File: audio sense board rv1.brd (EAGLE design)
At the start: 130.8 x 26.7 mm, 33 parts, among them IC2 TSOP38238, J1 PJRAN1X1U01X, J2 PJRAN1X1U01X, Q1 2N3904, Q2 2N3904

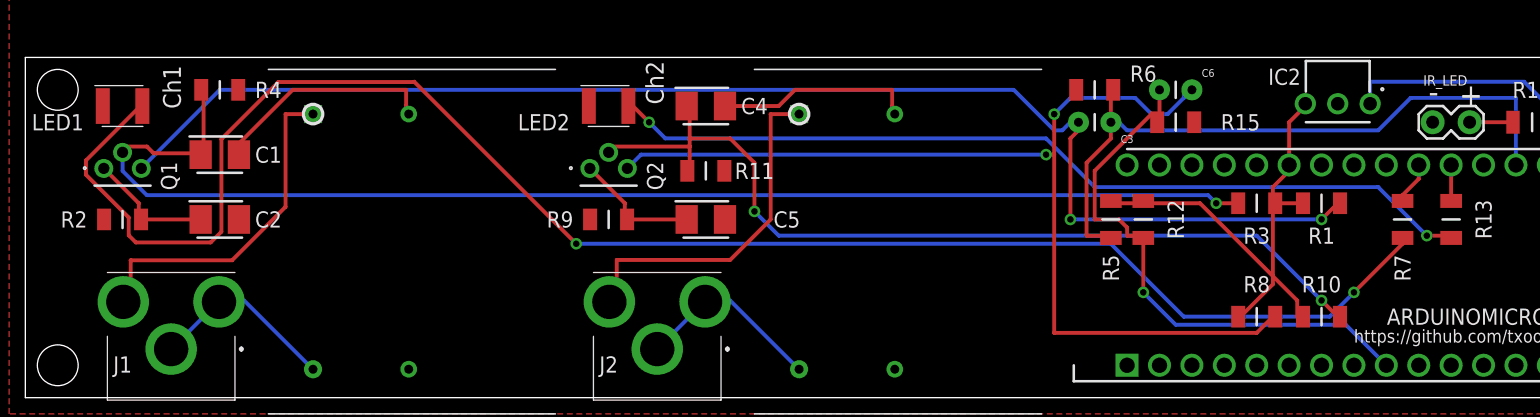
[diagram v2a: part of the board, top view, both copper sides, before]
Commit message: increase pad size for all resistors
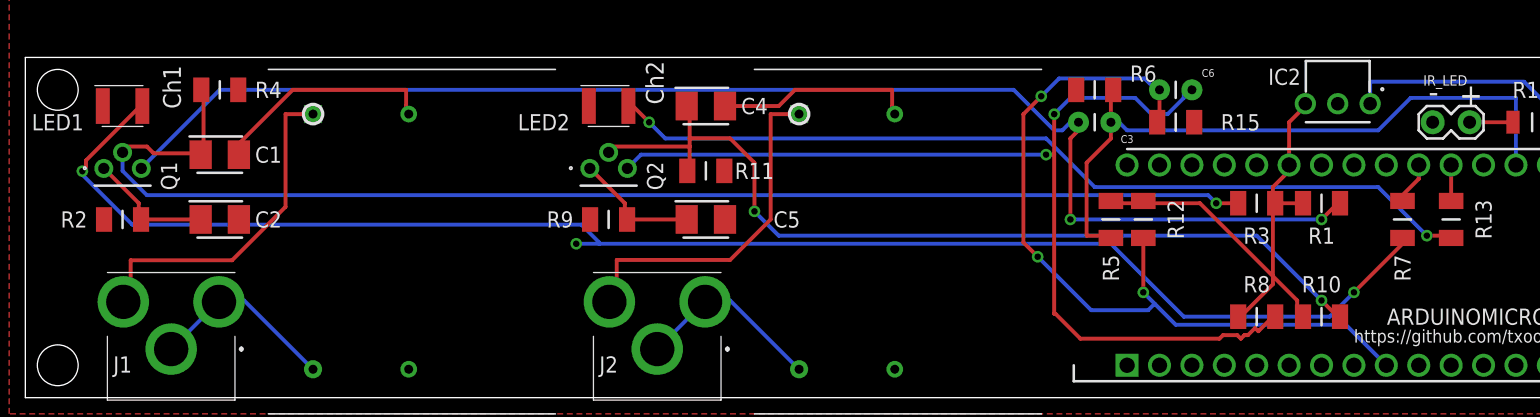
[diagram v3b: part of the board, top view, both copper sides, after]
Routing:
- net CHAN2: track 44.7 -> 64.0 mm, vias 1 -> 3
- net N$4: track 133.4 -> 120.3 mm, vias 2 -> 3
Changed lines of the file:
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@@
 <layers>
 <layer number="1" name="Top" color="4" fill="1" visible="yes" active="yes"/>
-<layer number="16" name="Bottom" color="1" fill="1" visible="no" active="yes"/>
+<layer number="16" name="Bottom" color="1" fill="1" visible="yes" active="yes"/>
 <layer number="17" name="Pads" color="2" fill="1" visible="yes" active="yes"/>
 <layer number="18" name="Vias" color="2" fill="1" visible="yes" active="yes"/>
@@
 <contactref element="R15" pad="2"/>
 <contactref element="C6" pad="1"/>
-<wire x1="86.36" y1="11.43" x2="87.63" y2="11.43" width="0.3048" layer="1"/>
-<wire x1="86.36" y1="12.065" x2="86.36" y2="11.43" width="0.3048" layer="1"/>
-<wire x1="85.725" y1="12.7" x2="86.36" y2="12.065" width="0.3048" layer="1"/>
-<wire x1="83.82" y1="12.7" x2="85.725" y2="12.7" width="0.3048" layer="1"/>
-<wire x1="83.82" y1="16.51" x2="83.82" y2="12.7" width="0.3048" layer="1"/>
-<wire x1="88.265" y1="20.955" x2="83.82" y2="16.51" width="0.3048" layer="1"/>
-<wire x1="88.9" y1="20.955" x2="88.265" y2="20.955" width="0.3048" layer="1"/>
 <wire x1="88.9" y1="20.32" x2="88.9" y2="20.955" width="0.3048" layer="1"/>
-<wire x1="87.63" y1="11.43" x2="87.63" y2="11.25" width="0.3048" layer="1"/>
 <wire x1="88.9" y1="20.32" x2="88.72" y2="20.32" width="0.3048" layer="1"/>
 <wire x1="88.9" y1="20.955" x2="88.9" y2="22.86" width="0.3048" layer="1"/>
@@
 <wire x1="103.505" y1="4.445" x2="106.68" y2="1.27" width="0.3048" layer="16"/>
 <wire x1="90.17" y1="4.445" x2="103.505" y2="4.445" width="0.3048" layer="16"/>
-<wire x1="87.63" y1="6.985" x2="90.17" y2="4.445" width="0.3048" layer="16"/>
+<wire x1="87.63" y1="6.985" x2="88.519" y2="6.096" width="0.3048" layer="16"/>
+<wire x1="88.519" y1="6.096" x2="90.17" y2="4.445" width="0.3048" layer="16"/>
 <wire x1="87.63" y1="11.25" x2="87.63" y2="6.985" width="0.3048" layer="1"/>
 <via x="87.63" y="6.985" extent="1-16" drill="0.508"/>
+<wire x1="88.5698" y1="22.9108" x2="88.8492" y2="22.9108" width="0.3048" layer="16"/>
+<wire x1="87.7316" y1="23.749" x2="88.5698" y2="22.9108" width="0.3048" layer="16"/>
+<wire x1="81.026" y1="23.749" x2="87.7316" y2="23.749" width="0.3048" layer="16"/>
+<wire x1="79.629" y1="22.352" x2="81.026" y2="23.749" width="0.3048" layer="16"/>
+<wire x1="78.232" y1="20.955" x2="79.629" y2="22.352" width="0.3048" layer="1"/>
+<wire x1="78.232" y1="10.8966" x2="78.232" y2="20.955" width="0.3048" layer="1"/>
+<wire x1="79.3496" y1="9.779" x2="78.232" y2="10.8966" width="0.3048" layer="1"/>
+<wire x1="83.5406" y1="5.588" x2="79.3496" y2="9.779" width="0.3048" layer="16"/>
+<wire x1="88.011" y1="5.588" x2="83.5406" y2="5.588" width="0.3048" layer="16"/>
+<wire x1="88.519" y1="6.096" x2="88.011" y2="5.588" width="0.3048" layer="16"/>
+<wire x1="88.8492" y1="22.9108" x2="88.9" y2="22.86" width="0.3048" layer="16"/>
+<via x="79.629" y="22.352" extent="1-16" drill="0.508"/>
+<via x="79.3496" y="9.779" extent="1-16" drill="0.508"/>
 </signal>
 <signal name="IRREC">
@@
 <wire x1="90.805" y1="5.08" x2="102.235" y2="5.08" width="0.3048" layer="16"/>
 <wire x1="85.09" y1="10.795" x2="90.805" y2="5.08" width="0.3048" layer="16"/>
-<wire x1="43.18" y1="10.795" x2="85.09" y2="10.795" width="0.3048" layer="16"/>
-<wire x1="30.48" y1="23.495" x2="43.18" y2="10.795" width="0.3048" layer="1"/>
+<wire x1="43.18" y1="10.795" x2="44.9834" y2="10.795" width="0.3048" layer="16"/>
+<wire x1="44.9834" y1="10.795" x2="85.09" y2="10.795" width="0.3048" layer="16"/>
 <wire x1="107.95" y1="10.795" x2="107.95" y2="11.25" width="0.3048" layer="1"/>
 <via x="104.14" y="6.985" extent="1-16" drill="0.508"/>
 <via x="43.18" y="10.795" extent="1-16" drill="0.508"/>
 <wire x1="4.7498" y1="17.3228" x2="8.9408" y2="21.5138" width="0.3048" layer="1"/>
-<wire x1="4.7498" y1="16.2052" x2="4.7498" y2="17.3228" width="0.3048" layer="1"/>
-<wire x1="8.1026" y1="12.8524" x2="4.7498" y2="16.2052" width="0.3048" layer="1"/>
-<wire x1="8.1026" y1="11.4554" x2="8.1026" y2="12.8524" width="0.3048" layer="1"/>
-<wire x1="8.6614" y1="10.8966" x2="8.1026" y2="11.4554" width="0.3048" layer="1"/>
-<wire x1="14.5288" y1="10.8966" x2="8.6614" y2="10.8966" width="0.3048" layer="1"/>
-<wire x1="15.367" y1="11.7348" x2="14.5288" y2="10.8966" width="0.3048" layer="1"/>
-<wire x1="15.367" y1="18.9992" x2="15.367" y2="11.7348" width="0.3048" layer="1"/>
-<wire x1="19.8374" y1="23.4696" x2="15.367" y2="18.9992" width="0.3048" layer="1"/>
-<wire x1="30.4546" y1="23.4696" x2="19.8374" y2="23.4696" width="0.3048" layer="1"/>
+<wire x1="4.7498" y1="16.4846" x2="4.7498" y2="17.3228" width="0.3048" layer="1"/>
 <wire x1="8.9408" y1="21.5138" x2="9.17" y2="21.59" width="0.3048" layer="1"/>
-<wire x1="30.4546" y1="23.4696" x2="30.48" y2="23.495" width="0.3048" layer="1"/>
+<wire x1="4.4704" y1="16.4846" x2="4.7498" y2="16.4846" width="0.3048" layer="1"/>
+<wire x1="4.4704" y1="16.2052" x2="4.4704" y2="16.4846" width="0.3048" layer="16"/>
+<wire x1="8.382" y1="12.2936" x2="4.4704" y2="16.2052" width="0.3048" layer="16"/>
+<wire x1="43.5864" y1="12.2936" x2="8.382" y2="12.2936" width="0.3048" layer="16"/>
+<wire x1="44.9834" y1="10.8966" x2="43.5864" y2="12.2936" width="0.3048" layer="16"/>
+<wire x1="44.9834" y1="10.8966" x2="44.9834" y2="10.795" width="0.3048" layer="16"/>
+<via x="4.4704" y="16.4846" extent="1-16" drill="0.508"/>
 </signal>
 <signal name="STATUS_CH1">
@@
 <contactref element="R8" pad="1"/>
 <contactref element="C6" pad="2"/>
-<wire x1="96.52" y1="3.81" x2="97.79" y2="5.08" width="0.3048" layer="1"/>
-<wire x1="80.645" y1="3.81" x2="96.52" y2="3.81" width="0.3048" layer="1"/>
+<wire x1="96.647" y1="3.937" x2="97.79" y2="5.08" width="0.3048" layer="1"/>
 <wire x1="80.645" y1="20.955" x2="80.645" y2="17.78" width="0.3048" layer="1"/>
-<wire x1="80.645" y1="17.78" x2="80.645" y2="3.81" width="0.3048" layer="1"/>
+<wire x1="80.645" y1="17.78" x2="80.645" y2="5.3086" width="0.3048" layer="1"/>
 <wire x1="81.915" y1="22.225" x2="80.645" y2="20.955" width="0.3048" layer="16"/>
 <wire x1="86.995" y1="22.225" x2="81.915" y2="22.225" width="0.3048" layer="16"/>
 <wire x1="88.265" y1="20.955" x2="86.995" y2="22.225" width="0.3048" layer="16"/>
-<wire x1="89.535" y1="20.955" x2="88.265" y2="20.955" width="0.3048" layer="16"/>
 <wire x1="90.805" y1="22.225" x2="89.535" y2="20.955" width="0.3048" layer="16"/>
 <wire x1="90.805" y1="22.86" x2="90.805" y2="22.225" width="0.3048" layer="16"/>
@@
 <via x="80.645" y="20.955" extent="1-16" drill="0.508"/>
 <via x="80.01" y="17.78" extent="1-16" drill="0.508"/>
+<wire x1="96.393" y1="4.191" x2="96.647" y2="3.937" width="0.3048" layer="1"/>
+<wire x1="95.8342" y1="3.6322" x2="96.393" y2="4.191" width="0.3048" layer="1"/>
+<wire x1="95.5548" y1="3.6322" x2="95.8342" y2="3.6322" width="0.3048" layer="1"/>
+<wire x1="95.2754" y1="3.3528" x2="95.5548" y2="3.6322" width="0.3048" layer="1"/>
+<wire x1="94.996" y1="3.6322" x2="95.2754" y2="3.3528" width="0.3048" layer="1"/>
+<wire x1="93.8784" y1="3.6322" x2="94.996" y2="3.6322" width="0.3048" layer="1"/>
+<wire x1="93.599" y1="3.3528" x2="93.8784" y2="3.6322" width="0.3048" layer="1"/>
+<wire x1="82.7024" y1="3.3528" x2="93.599" y2="3.3528" width="0.3048" layer="1"/>
+<wire x1="80.7466" y1="5.3086" x2="82.7024" y2="3.3528" width="0.3048" layer="1"/>
+<wire x1="80.7466" y1="5.3086" x2="80.645" y2="5.3086" width="0.3048" layer="1"/>
+<wire x1="88.265" y1="20.955" x2="89.535" y2="20.955" width="0.3048" layer="16"/>
 </signal>
 </signals>

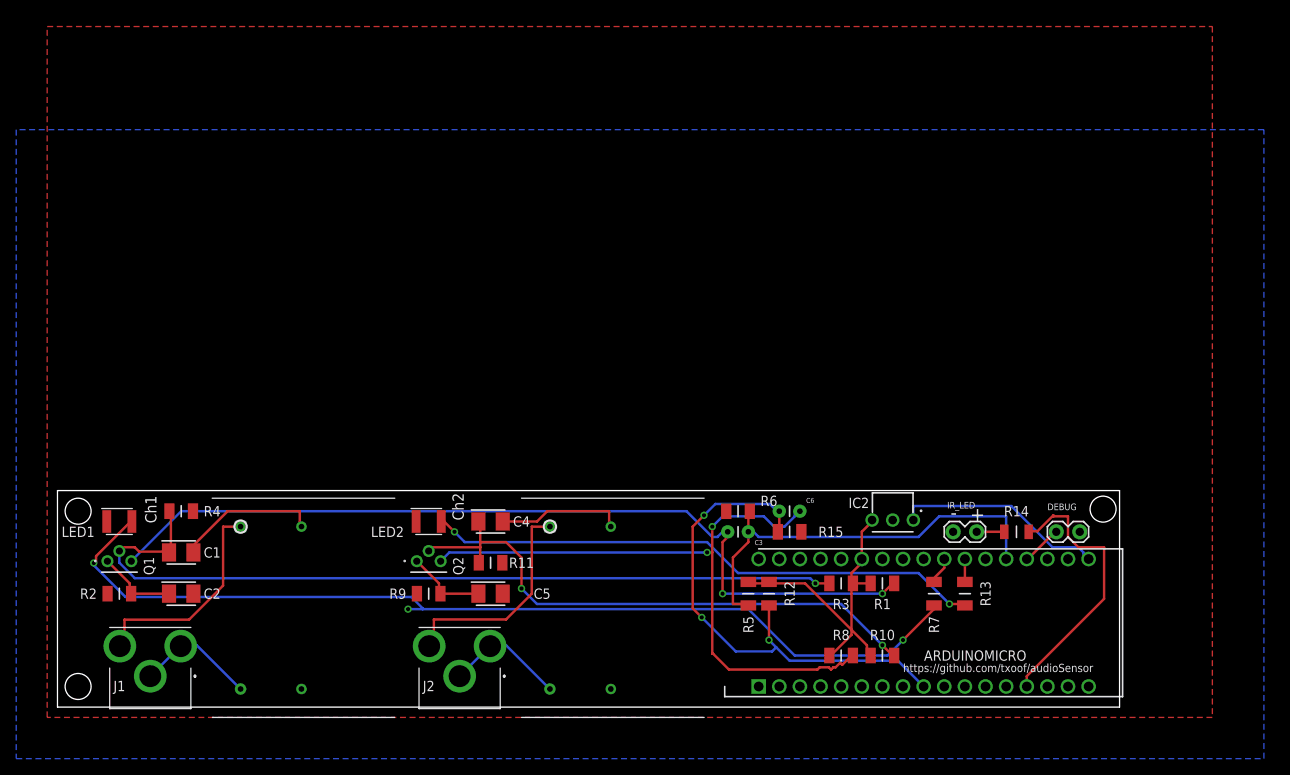
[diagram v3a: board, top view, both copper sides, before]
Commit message: update pad sizes
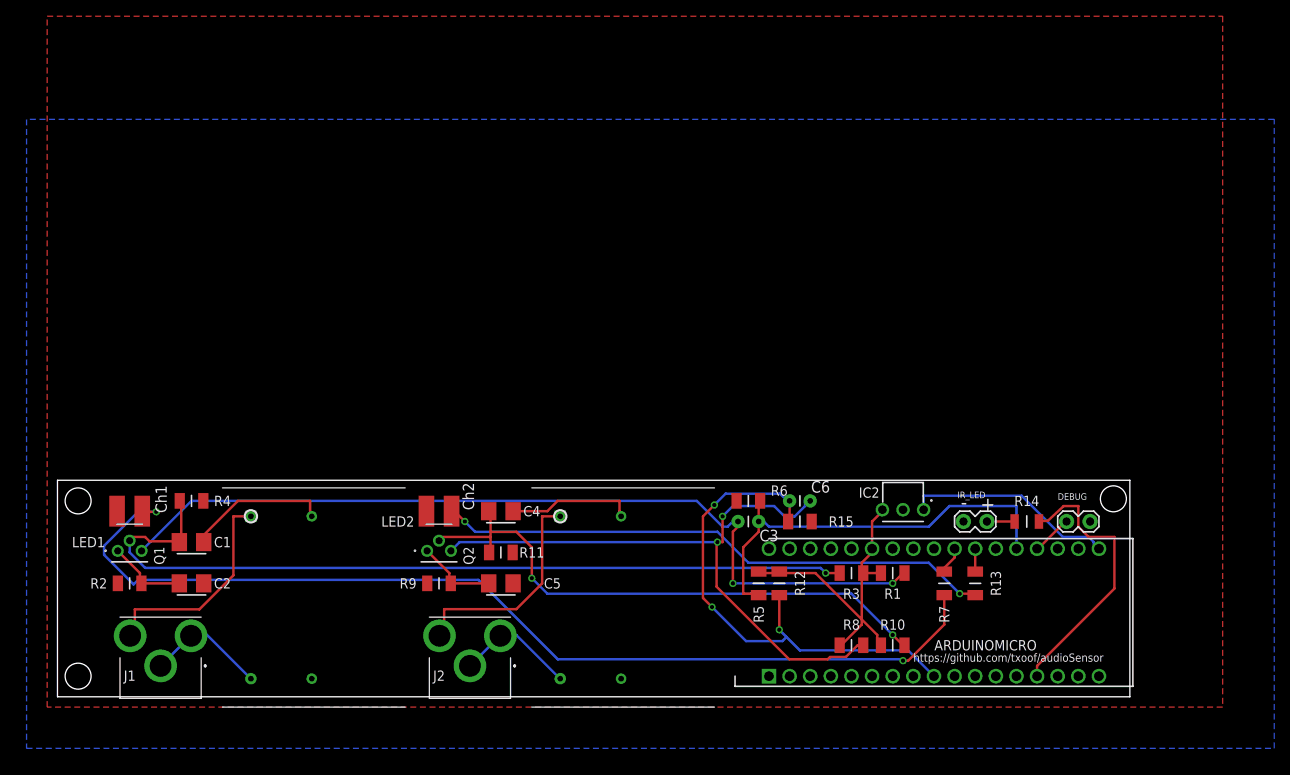
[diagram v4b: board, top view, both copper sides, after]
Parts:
- moved R12 1.80 mm to (88.9, 14.0)
- moved C3 1.80 mm to (85.1, 21.6)
- moved R1 1.80 mm to (102.9, 15.2)
- moved R10 1.80 mm to (102.9, 6.35)
- moved R3 1.80 mm to (97.8, 15.2)
- moved R6 1.80 mm to (85.1, 24.1)
- moved R8 1.80 mm to (97.8, 6.35)
- moved R9 1.80 mm to (47.0, 14.0)
- moved L2 1.80 mm to (58.4, -1.27)
- moved C2 1.80 mm to (16.5, 14.0)
- moved LED2 1.80 mm to (47.0, 22.9)
- moved Q2 1.80 mm to (47.0, 20.3)
- moved R2 1.80 mm to (8.89, 14.0)
- moved C1 1.80 mm to (16.5, 19.1)
- moved R4 1.80 mm to (16.5, 24.1)
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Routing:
- net N$4: track 120.3 -> 125.9 mm, vias 3 -> 2
- net N$8: track 81.9 -> 78.1 mm
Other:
- board size 130.8 x 26.7 mm -> 132.1 x 26.7 mm

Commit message: update pads R14
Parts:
- R14: device Samac Populated:RESC3216X60N -> Samac Populated:RESC3116X70N
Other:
- board text added: "https://github.com/txoof/audioSensor RV 1"
- board text removed: "https://github.com/txoof/audioSensor"
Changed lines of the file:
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@@
 <text x="51.308" y="22.987" size="1.397" layer="21" rot="R90">Ch2</text>
 <text x="12.065" y="26.035" size="1.397" layer="21" rot="R270">Ch1</text>
-<text x="105.41" y="4.318" size="1.016" layer="25">https://github.com/txoof/audioSensor</text>
+<text x="106.68" y="6.858" size="1.016" layer="25">https://github.com/txoof/audioSensor
+RV 1</text>
 <wire x1="0" y1="0" x2="0" y2="26.67" width="0.000253125" layer="20"/>
 <wire x1="0" y1="26.67" x2="132.08" y2="26.67" width="0.000253125" layer="20"/>
@@
 <attribute name="MOUSER_PART_NUMBER" value="782-A000053" x="146.05" y="-21.59" size="1.778" layer="27" display="off"/>
 <attribute name="MOUSER_PRICE-STOCK" value="https://www.mouser.com/Search/Refine.aspx?Keyword=782-A000053" x="146.05" y="-21.59" size="1.778" layer="27" display="off"/>
-<attribute name="NAME" x="114.3" y="6.35" size="1.27" layer="25" rot="R180" align="center"/>
+<attribute name="NAME" x="130.81" y="10.16" size="1.27" layer="25" rot="R270" align="center"/>
 <attribute name="RS_PART_NUMBER" value="7717667" x="146.05" y="-21.59" size="1.778" layer="27" display="off"/>
 <attribute name="RS_PRICE-STOCK" value="http://uk.rs-online.com/web/p/products/7717667" x="146.05" y="-21.59" size="1.778" layer="27" display="off"/>
@@
 <attribute name="VALUE" x="115.57" y="23.622" size="0.6096" layer="27" font="vector" ratio="20" rot="R180"/>
 </element>
-<element name="R14" library="Samac Populated" package="RESC3216X60N" value="100" x="119.38" y="21.59" smashed="yes">
-<attribute name="DESCRIPTION" value="Thick Film Resistors - SMD 1/4Watt 100ohms 5% Commercial Use" x="170.18" y="-40.64" size="1.778" layer="27" display="off"/>
-<attribute name="HEIGHT" value="0.6mm" x="170.18" y="-40.64" size="1.778" layer="27" display="off"/>
-<attribute name="MANUFACTURER_NAME" value="Vishay" x="170.18" y="-40.64" size="1.778" layer="27" display="off"/>
-<attribute name="MANUFACTURER_PART_NUMBER" value="CRCW1206100RJNEAC" x="170.18" y="-40.64" size="1.778" layer="27" display="off"/>
-<attribute name="MOUSER_PART_NUMBER" value="71-CRCW1206100RJNEAC" x="170.18" y="-40.64" size="1.778" layer="27" display="off"/>
-<attribute name="MOUSER_PRICE-STOCK" value="https://www.mouser.com/Search/Refine.aspx?Keyword=71-CRCW1206100RJNEAC" x="170.18" y="-40.64" size="1.778" layer="27" display="off"/>
+<element name="R14" library="Samac Populated" package="RESC3116X70N" value="100" x="119.38" y="21.59" smashed="yes">
+<attribute name="ALLIED_NUMBER" value="70265175" x="119.38" y="21.59" size="1.778" layer="27" display="off"/>
+<attribute name="ALLIED_PRICE-STOCK" value="https://www.alliedelec.com/panasonic-erj-8geyj101v/70265175/" x="119.38" y="21.59" size="1.778" layer="27" display="off"/>
+<attribute name="DESCRIPTION" value="PANASONIC ELECTRONIC COMPONENTS - ERJ8GEYJ101V - RES, THICK FILM, 100R, 5%, 0.25W, 1206" x="170.18" y="-40.64" size="1.778" layer="27" display="off"/>
+<attribute name="HEIGHT" value="0.7mm" x="170.18" y="-40.64" size="1.778" layer="27" display="off"/>
+<attribute name="MANUFACTURER_NAME" value="Panasonic" x="170.18" y="-40.64" size="1.778" layer="27" display="off"/>
+<attribute name="MANUFACTURER_PART_NUMBER" value="ERJ8GEYJ101V" x="170.18" y="-40.64" size="1.778" layer="27" display="off"/>
+<attribute name="MOUSER_PART_NUMBER" value="" x="170.18" y="-40.64" size="1.778" layer="27" display="off"/>
+<attribute name="MOUSER_PRICE-STOCK" value="" x="170.18" y="-40.64" size="1.778" layer="27" display="off"/>
 <attribute name="NAME" x="119.38" y="24.13" size="1.27" layer="25" align="center"/>
 <attribute name="RS_PART_NUMBER" value="" x="170.18" y="-40.64" size="1.778" layer="27" display="off"/>
@@
 <attribute name="MOUSER_PART_NUMBER" value="859-LTST-C930KRKT" x="8.89" y="22.86" size="1.778" layer="27" display="off"/>
 <attribute name="MOUSER_PRICE-STOCK" value="https://www.mouser.com/Search/Refine.aspx?Keyword=859-LTST-C930KRKT" x="8.89" y="22.86" size="1.778" layer="27" display="off"/>
-<attribute name="NAME" x="3.81" y="19.05" size="1.27" layer="25" rot="R180" align="center"/>
+<attribute name="NAME" x="5.08" y="22.86" size="1.27" layer="25" rot="R90" align="center"/>
 <attribute name="RS_PART_NUMBER" value="1689768" x="8.89" y="22.86" size="1.778" layer="27" display="off"/>
 <attribute name="RS_PRICE-STOCK" value="http://uk.rs-online.com/web/p/products/1689768" x="8.89" y="22.86" size="1.778" layer="27" display="off"/>
@@
 <attribute name="MOUSER_PART_NUMBER" value="859-LTST-C930KRKT" x="46.99" y="22.86" size="1.778" layer="27" display="off"/>
 <attribute name="MOUSER_PRICE-STOCK" value="https://www.mouser.com/Search/Refine.aspx?Keyword=859-LTST-C930KRKT" x="46.99" y="22.86" size="1.778" layer="27" display="off"/>
-<attribute name="NAME" x="41.91" y="21.59" size="1.27" layer="25" rot="R180" align="center"/>
+<attribute name="NAME" x="43.18" y="22.86" size="1.27" layer="25" rot="R270" align="center"/>
 <attribute name="RS_PART_NUMBER" value="1689768" x="46.99" y="22.86" size="1.778" layer="27" display="off"/>
 <attribute name="RS_PRICE-STOCK" value="http://uk.rs-online.com/web/p/products/1689768" x="46.99" y="22.86" size="1.778" layer="27" display="off"/>
@@
 <contactref element="IR_LED" pad="1"/>
 <contactref element="R14" pad="1"/>
-<wire x1="114.4778" y1="21.59" x2="117.88" y2="21.59" width="0.3048" layer="1"/>
+<wire x1="114.4778" y1="21.59" x2="117.93" y2="21.59" width="0.3048" layer="1"/>
 </signal>
 <signal name="VCC">
@@
 <wire x1="130.175" y1="19.685" x2="127" y2="19.685" width="0.3048" layer="1"/>
 <wire x1="121.1326" y1="21.6662" x2="121.9708" y2="21.6662" width="0.3048" layer="1"/>
-<wire x1="121.1326" y1="21.6662" x2="120.88" y2="21.59" width="0.3048" layer="1"/>
+<wire x1="121.1326" y1="21.6662" x2="120.83" y2="21.59" width="0.3048" layer="1"/>
 <wire x1="121.9708" y1="21.6662" x2="123.9266" y2="23.495" width="0.3048" layer="1"/>
 </signal>
@@
 </drawing>
 <compatibility>
+<note version="6.3" minversion="6.2.2" severity="warning">
+Since Version 6.2.2 text objects can contain more than one line,
+which will not be processed correctly with this version.
+</note>
 <note version="8.2" severity="warning">
 Since Version 8.2, EAGLE supports online libraries. The ids
